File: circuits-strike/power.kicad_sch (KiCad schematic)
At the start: 13 parts, among them U3 REG_AMS1117-3.3, U4 TPS5430DDAR

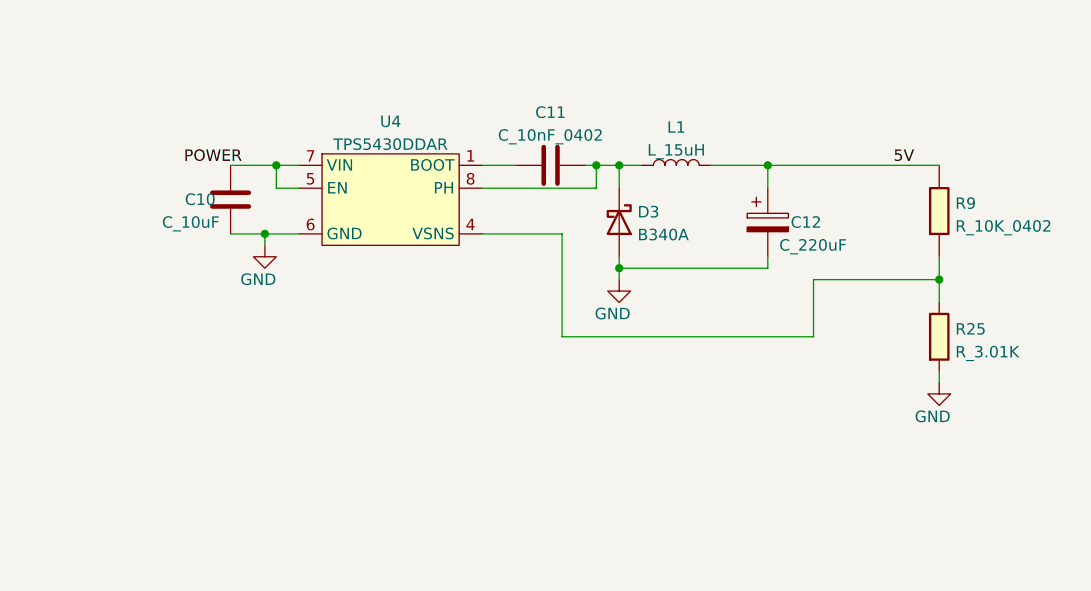
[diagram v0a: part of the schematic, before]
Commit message: Finished schematic for shrinking PCB for residential systems
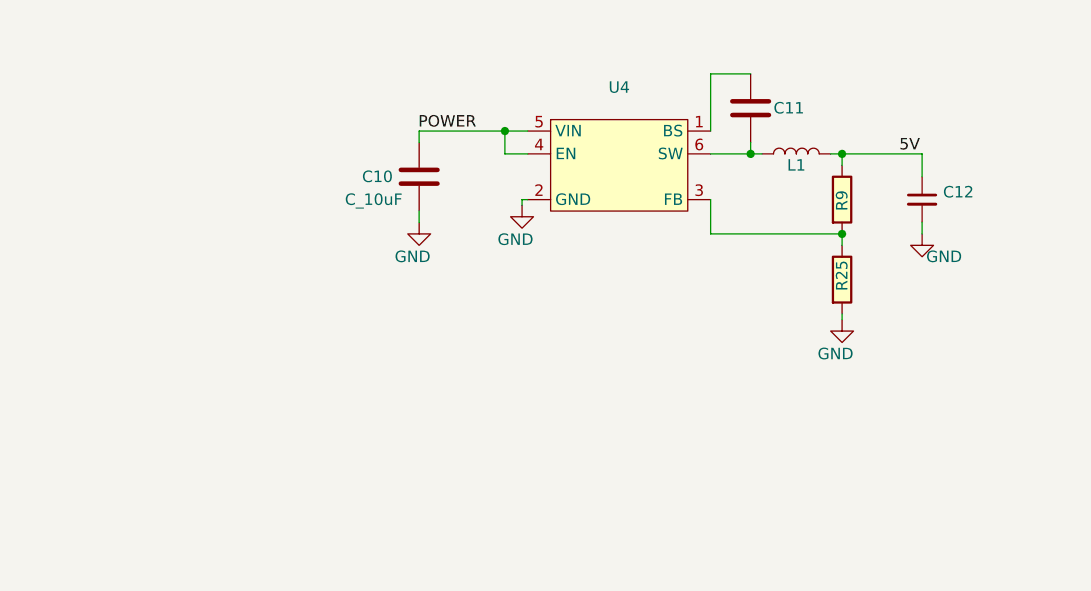
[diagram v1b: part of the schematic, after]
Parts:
- removed C11: C_10nF_0402, Capacitor_SMD:C_0402_1005Metric, symbol Open Automation:C_10nF_0402
- removed C12: C_220uF, Capacitor_SMD:CP_Elec_10x10, symbol Open Automation:C_220uF
- removed D3: B340A, Diode_SMD:D_SMA, symbol Open Automation:B340A
- removed L1: L_15uH, Open_Automation:L_CD54, symbol Open Automation:L_15uH
- removed R25: R_3.01K, Resistor_SMD:R_0402_1005Metric_Pad0.72x0.64mm_HandSolder, symbol Open Automation:R_3.01K
- removed R9: R_10K_0402, Resistor_SMD:R_0402_1005Metric_Pad0.72x0.64mm_HandSolder, symbol Open Automation:R_10K_0402
- removed U4: TPS5430DDAR, Package_SO:SOIC-8-1EP_3.9x4.9mm_P1.27mm_EP2.514x3.2mm_ThermalVias, symbol Open Automation:TPS5430DDAR
- added C11: (no value), symbol Open Automation:C_22nF
- added C12: (no value), symbol Open Automation:C_22uF
- added L1: (no value), symbol Open Automation:L_10uH
- added R25: (no value), symbol Open Automation:R_19K
- added R9: (no value), symbol Open Automation:R_49.9K
- added U4: (no value), symbol Open Automation:REG_MT2492
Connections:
- net 5V: now also C12.1, L1.2, R9.1
- net GND: now also C12.2, R25.2, U4.2 (GND)
- net POWER: now also U4.4 (EN), U4.5 (VIN)
- new net: C11.2, L1.1, U4.6 (SW)
- new net: C11.1, U4.1 (BS)
- new net: R25.1, R9.2, U4.3 (FB)
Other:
- moved on the sheet: C10
